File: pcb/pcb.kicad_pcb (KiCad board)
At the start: 2 copper layers, 63 x 60 mm, 72 parts, among them CN10 1x2, CN2 1x8, CN3 1x8, CN4 1x8, CN5 1x4, CN6 1x2, CN7 1x2, CN9 2x5, IC1 AP2112K-3.3TRG1, IC2 STM32f103C8T, IC3 INA199B2, IC4 AP62300TWU-7, IC5 MCP2551, SW1 switch_3x4, SW2 switch_3x4, SW3 219-3LPST

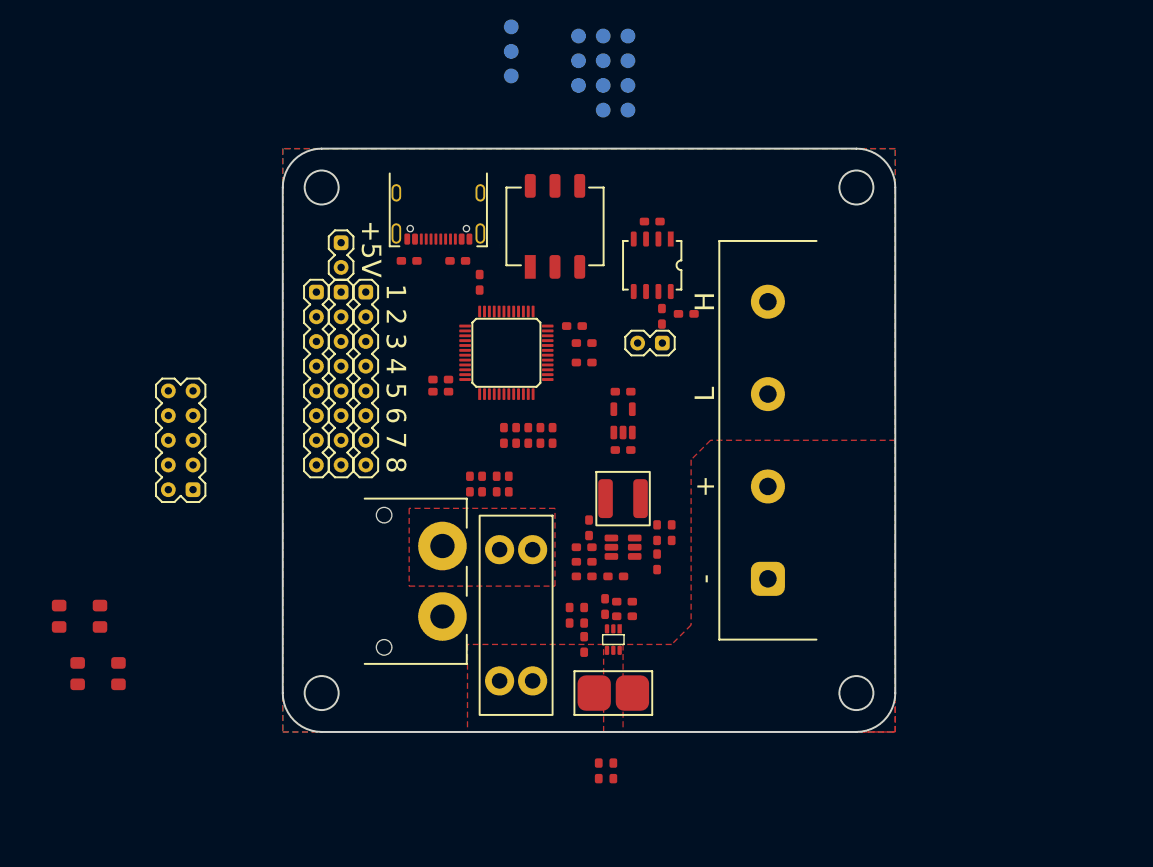
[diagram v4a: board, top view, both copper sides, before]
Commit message: added missing footprints
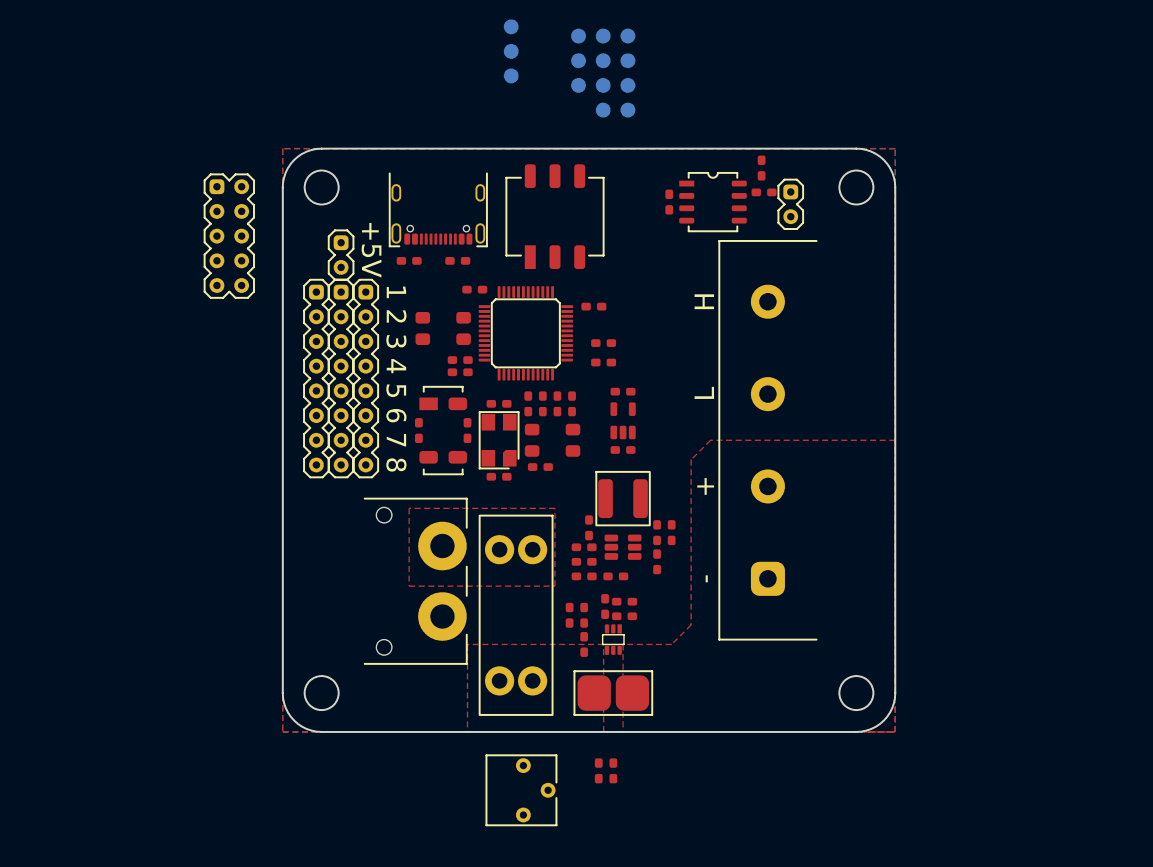
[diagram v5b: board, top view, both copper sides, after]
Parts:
- added R10: 100k, potentiometers:3362P, F.Cu at (123.8, 136.0)
- added X1: H130B-8.000-18-3030-EXT-TR, xtal:5x3.2, F.Cu at (121.2, 100.0)
- added X2: 32.768K12.5PI/MC306, xtal:8x3.2, F.Cu at (115.5, 99.0)
- moved SW2 51.9 mm to (126.8, 100.0)
- moved SW1 50.2 mm to (115.5, 88.5)
- moved CN9 31.3 mm to (92.2, 73.9), turned to 0 degrees
- moved CN10 20.4 mm to (151.2, 77.0), turned to 0 degrees
- moved R15 16.9 mm to (148.2, 72.0), turned to -90 degrees
- moved R14 16.5 mm to (148.5, 74.5), turned to 180 degrees
- moved IC5 9.02 mm to (143.2, 75.5), turned to 0 degrees
- moved C17 8.25 mm to (121.2, 96.2), turned to 0 degrees
- moved C18 7.60 mm to (113.0, 99.0)
- moved C19 5.70 mm to (118.0, 99.0)
- moved R3 4.96 mm to (125.5, 102.8), turned to 0 degrees
- moved C14 4.42 mm to (127.2, 96.2)
- moved R16 3.82 mm to (128.8, 96.2)
- moved C20 3.48 mm to (124.2, 96.2)
- moved C15 3.26 mm to (125.8, 96.2)
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
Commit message: worked on layout
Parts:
- added C8: 100n, SMT:0603, F.Cu at (131.7, 118.0)
- moved R11 63.8 mm to (72.5, 113.8), turned to 90 degrees
- moved TP7 62.6 mm to (76.1, 89.4)
- moved TP8 60.4 mm to (81.2, 89.4)
- moved TP6 59.2 mm to (76.1, 84.3)
- moved C22 58.4 mm to (76.2, 115.0), turned to 90 degrees
- moved C3 45.9 mm to (82.8, 114.0)
- moved R1 45.9 mm to (84.2, 114.0)
- moved R2 45.9 mm to (84.2, 117.0)
- moved TP4 40.1 mm to (116.8, 94.4)
- moved TP14 39.9 mm to (116.8, 97.0), turned to 90 degrees
- moved TP13 37.1 mm to (119.3, 97.0), turned to 90 degrees
- moved TP8 34.9 mm to (114.2, 91.9)
- moved TP12 34.5 mm to (121.8, 97.0), turned to 90 degrees
- moved CN9 34.2 mm to (111.7, 102.1), turned to 90 degrees
- moved TP5 32.5 mm to (119.3, 94.4)
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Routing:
- net Net-(IC2-OSC_IN): track 0.00 -> 14.7 mm
- net /MCU/NRST: track 0.00 -> 10.2 mm
- net Net-(IC2-OSC_OUT): track 0.00 -> 9.60 mm
- net Net-(IC2-OSC32_OUT): track 0.00 -> 8.42 mm
- net Net-(IC2-OSC32_IN): track 0.00 -> 8.40 mm
- net Net-(IC2-VDDA): track 0.00 -> 4.45 mm
- net /MCU/TX: track 0.00 -> 3.10 mm, vias 0 -> 1
- net /MCU/RX: track 0.00 -> 1.91 mm, vias 0 -> 1
- net GND: track 0.00 -> 1.50 mm, vias 0 -> 1

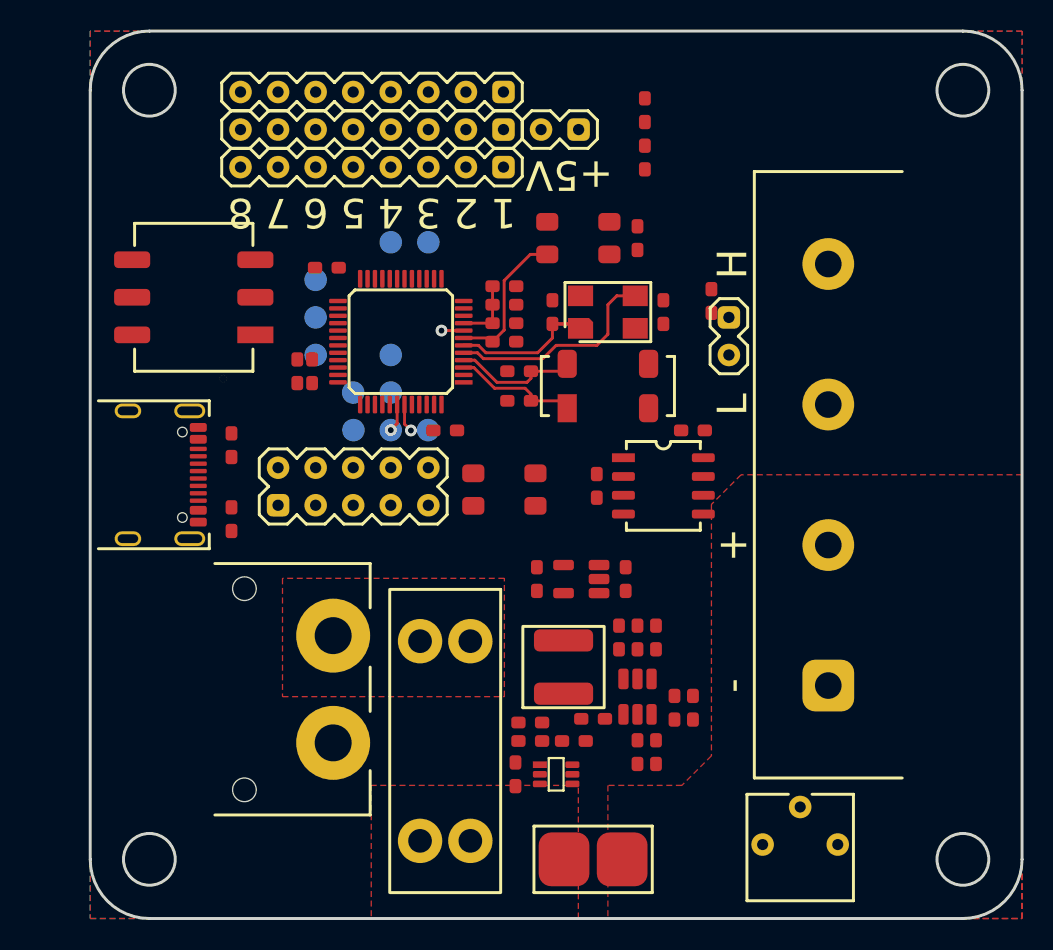
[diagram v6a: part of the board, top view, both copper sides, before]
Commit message: worked on layout. changed JTAG pinout and changed it to bottomside test-points
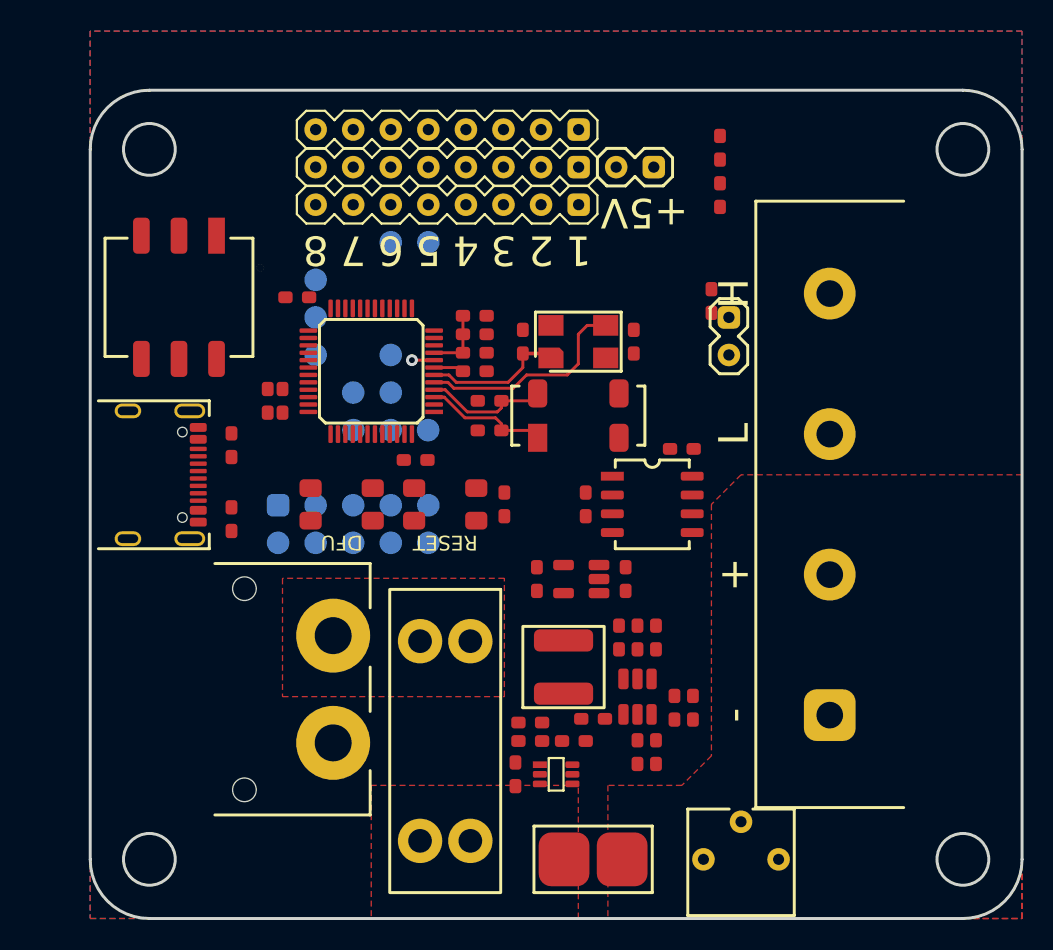
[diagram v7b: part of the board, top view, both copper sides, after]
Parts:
- CN9: footprint pin_headers:2x5 -> pin_headers:2x5_test_points; moved to B.Cu
- moved R3 20.1 mm to (127.0, 102.0), turned to -90 degrees
- moved SW2 20.1 mm to (123.0, 102.0), turned to 180 degrees
- moved SW1 11.0 mm to (116.0, 102.0)
- moved CN3 5.68 mm to (124.4, 79.2)
- moved CN7 5.68 mm to (134.6, 79.2)
- moved D1 5.68 mm to (141.6, 77.9)
- moved R4 5.68 mm to (141.6, 81.1)
- moved CN2 5.68 mm to (124.4, 81.7)
- moved CN4 5.68 mm to (124.4, 76.7)
- moved R10 4.12 mm to (143.0, 126.0)
- moved C10 2.83 mm to (112.0, 95.0)
- moved C11 2.83 mm to (113.0, 88.0)
- moved C12 2.83 mm to (121.0, 99.0)
- moved C13 2.83 mm to (111.0, 95.0)
- moved C14 2.83 mm to (125.0, 91.8)
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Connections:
- CN9 pad 5: GND -> 5V
- CN9 pad 9: GND -> unconnected-(CN9-Pad9)
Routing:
- net /MCU/NRST: track 10.2 -> 2.05 mm
- net /MCU/TX: track 3.10 -> 0.00 mm, vias 1 -> 0
- net /MCU/RX: track 1.91 -> 0.00 mm, vias 1 -> 0
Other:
- board size 63 x 60 mm -> 63 x 56 mm
- board text added: "DFU"
- board text added: "JTAG"
- board text added: "RESET"

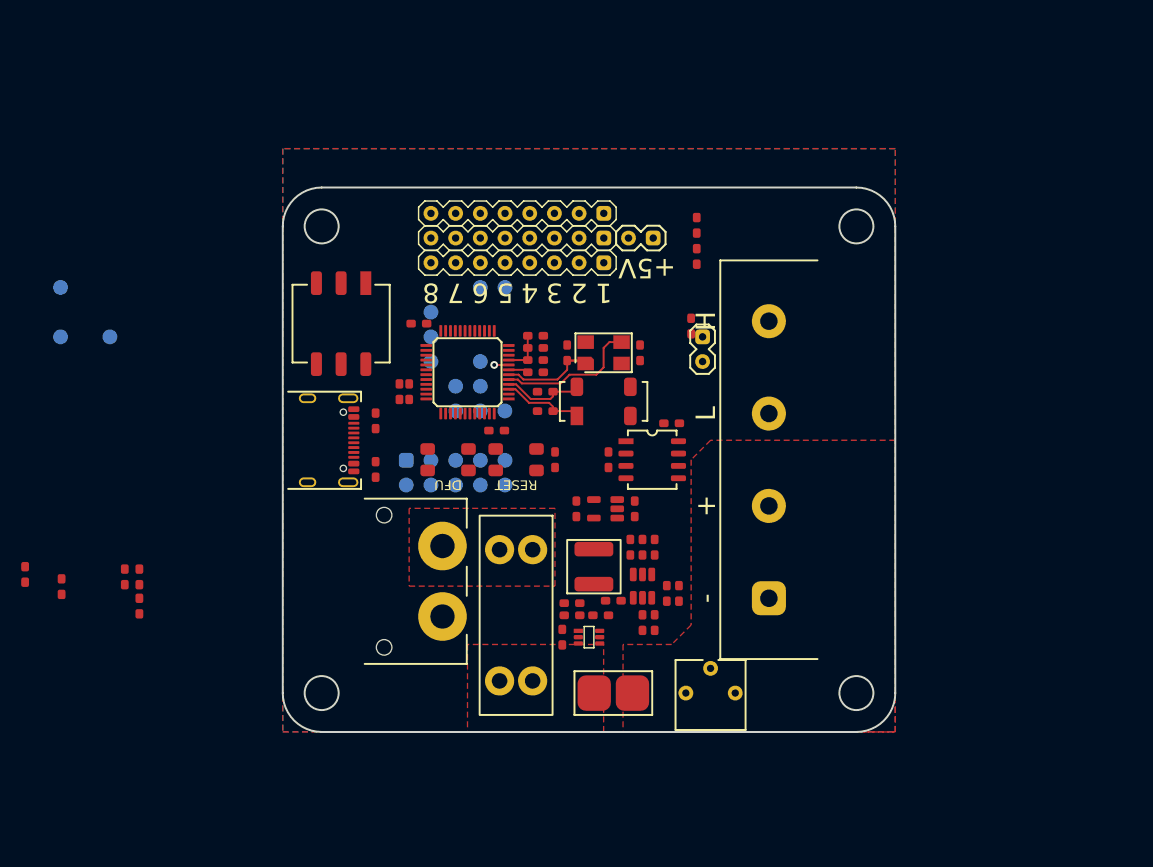
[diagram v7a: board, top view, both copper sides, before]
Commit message: removed RTC crystal, started routing
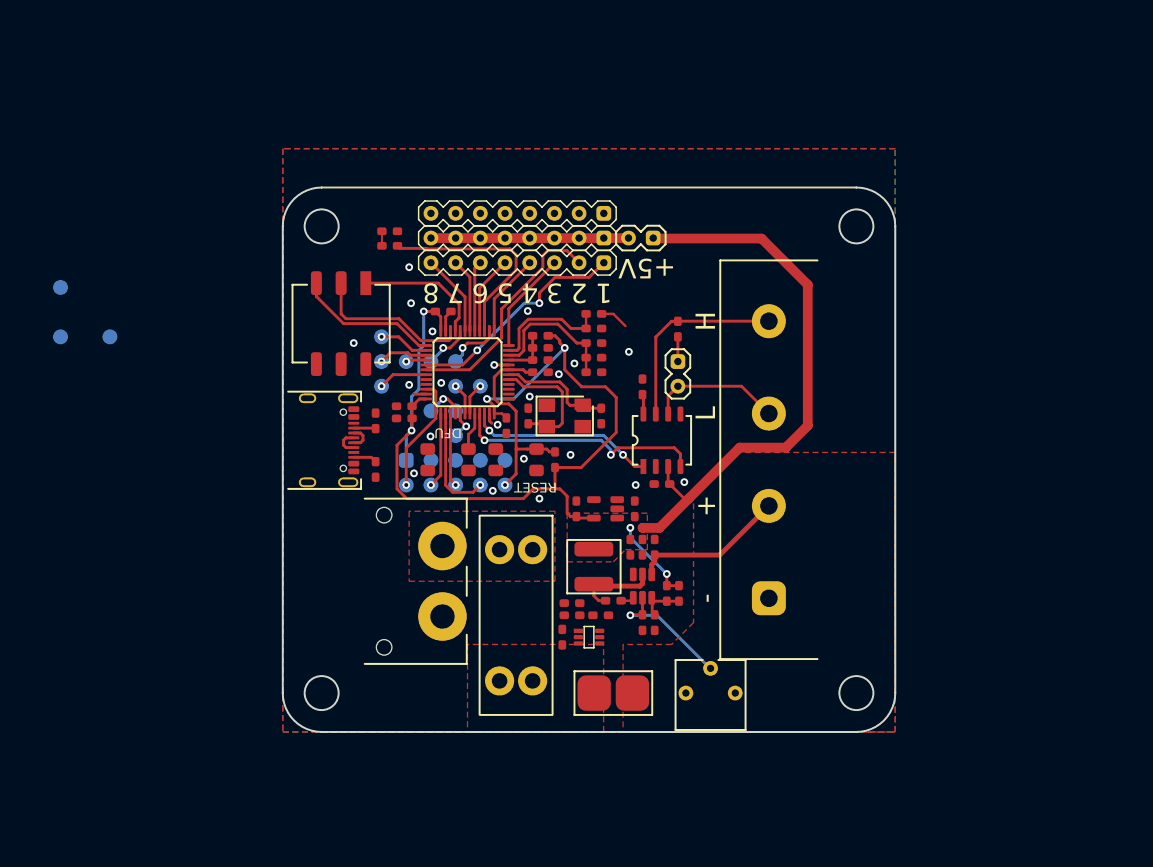
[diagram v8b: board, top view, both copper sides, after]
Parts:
- removed C18, C19: 22p, SMT:0603
- removed X2: 32.768K12.5PI/MC306, xtal:8x3.2
- moved R11 64.3 mm to (131.0, 87.0), turned to 0 degrees
- moved C22 60.8 mm to (131.0, 88.5), turned to 0 degrees
- moved C3 53.9 mm to (131.0, 90.0), turned to 0 degrees
- moved R2 52.6 mm to (131.0, 93.0), turned to 0 degrees
- moved R1 51.9 mm to (131.0, 91.5), turned to 180 degrees
- moved R4 31.6 mm to (110.0, 80.0), turned to 0 degrees
- moved D1 31.6 mm to (110.0, 78.5), turned to 0 degrees
- moved C17 13.2 mm to (124.2, 97.5), turned to 90 degrees
- moved TP2 10.5 mm to (109.2, 94.4)
- moved TP1 9.16 mm to (116.8, 91.9)
- moved TP3 9.16 mm to (114.2, 91.9)
- moved X1 7.63 mm to (128.0, 97.5), turned to 0 degrees
- moved C16 7.38 mm to (131.8, 97.5), turned to -90 degrees
- moved C24 6.04 mm to (138.0, 104.5), turned to 180 degrees
- moved TP6 5.68 mm to (109.2, 89.4)
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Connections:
- IC2 pad 3: Net-(IC2-OSC32_IN) -> unconnected-(IC2-OSC32_IN-Pad3)
- IC2 pad 4: Net-(IC2-OSC32_OUT) -> unconnected-(IC2-OSC32_OUT-Pad4)
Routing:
- net 3V3: track 0.00 -> 91.9 mm, vias 0 -> 4
- net 5V: track 0.00 -> 66.9 mm, vias 0 -> 2
- net /CAN/CAN_RX: track 0.00 -> 25.9 mm, vias 0 -> 2
- net /MCU/CH2: track 0.00 -> 23.8 mm
- net /MCU/CH1: track 0.00 -> 23.2 mm, vias 0 -> 2
- net /MCU/status: track 0.00 -> 21.7 mm
- net /Servo VCC: track 0.00 -> 20.3 mm
- net /CAN_H: track 0.00 -> 20.2 mm
- net /MCU/NRST: track 2.05 -> 21.5 mm, vias 0 -> 1
- net /CAN/CAN_TX: track 0.00 -> 19.3 mm, vias 0 -> 2
- net /MCU/ADDR2: track 0.00 -> 16.5 mm
- net /Battery: track 0.00 -> 16.0 mm
- net /MCU/ADDR3: track 0.00 -> 14.8 mm
- net /MCU/V_bat: track 0.00 -> 14.3 mm
- net /CAN_L: track 0.00 -> 13.8 mm
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- added copper zone on F.Cu, net 5V
